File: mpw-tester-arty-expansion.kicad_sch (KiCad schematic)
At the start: 111 parts

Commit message: Update MCP4661 symbol
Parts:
- removed J?: 61300611121, antmicro-footprints:61300611121, symbol antmicroRectangularConnectorsHeadersMalePins:61300611121
- removed U?: MCP4661, antmicro-footprints:QFN-16_EP_4x4_Pitch0.65mm, symbol antmicroInterfaceIOExpanders:MCP4661
- added J?: 61300611121, antmicro-footprints:61300611121, symbol antmicroRectangularConnectorsHeadersMalePins:61300611121
- added U?: MCP4661-103E/ML, antmicro-footprints:QFN-16_EP_4x4_Pitch0.65mm, symbol antmicroInterfaceIOExpanders:MCP4661-103E/ML
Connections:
- net AGND: now also U?.10 (P0B), U?.13 (A2), U?.14 (A1), U?.3 (VSS), U?.4 (VSS), U?.5 (P1B)
- net ARTY_SCL: now also U?.1 (SCL)
- net ARTY_SDA: now also U?.2 (SDA)
- net MEM.SCK: now also J?.2
- net MEM.SI: now also J?.3
- net MEM.SO: now also J?.4
- net MEM.~{CS}: now also J?.1
- net MEM.~{HOLD}: now also J?.6
- net MEM.~{WP}: now also J?.5
- net P0W: now also U?.9 (P0W)
- net P1W: now also U?.6 (P1W)
- net 5V0_SEL: now reaches C?.1, J?.1, R?.1, R?.1, R?.1, R?.1, R?.2, U?.1 (VIN)
- net 5V0_SEL: now also U?.15 (VDD)
- net at R?.1: now also U?.12 (~{WP})
- net at R?.2: now also U?.16 (HVC/A0)
- net 5V0: now reaches D?.K, D?.K, J?.2
- net 5V_ARTY renamed 5V0_ARTY
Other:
- moved on the sheet: C?, D?, J?, R?, U?

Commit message: Cleanup net names
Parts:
- removed J?: Conn_01x02, Connector_PinHeader_2.54mm:PinHeader_1x02_P2.54mm_Vertical, symbol Connector_Generic:Conn_01x02
- removed J?: 61300611121, antmicro-footprints:61300611121, symbol antmicroRectangularConnectorsHeadersMalePins:61300611121
- added C? (x2): C_100n_0402, antmicro-footprints:0402-cap, symbol antmicroCapacitors0402:C_100n_0402
- added C?: C_1u_0402, antmicro-footprints:0402-cap, symbol antmicroCapacitors0402:C_1u_0402
- added J?: 61300711121, antmicro-footprints:61300711121, symbol antmicroRectangularConnectorsHeadersMalePins:61300711121
- added J?: 61300311121, antmicro-footprints:PinHeader_1x3_P2.54_Drill1.1mm, symbol antmicroRectangularConnectorsHeadersMalePins:61300311121
- added NT? (x2): NetTie_2, antmicro-footprints:NetTie-2_SMD_Pad0.127mm, symbol antmicroShuntsJumpers:NetTie_2
- added U?: NTS0102GT, antmicro-footprints:PSON50P100X195X50-8N, symbol antmicroLogicTranslatorsLevelShifters:NTS0102GT
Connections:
- net gpio is gone; now on net CRVL_~{RST}: J?.4
- net ~{RST} is gone; now on net CRVL_GPIO: J?.2
- net +3V3: no longer J?.1
- net 5V0_SEL: now also C?.1, U?.7 (VCC_B)
- net AGND: now also C?.2, C?.2, C?.2, J?.7, U?.2 (GND)
- net ARTY_SCL: now also U?.8 (B1); no longer J?.47 (SCL)
- net ARTY_SDA: now also U?.1 (B2); no longer J?.48 (SDA)
- net ARTY_XCLK: now also J?.1
- net MEM.SCK: now also J?.2
- net MEM.SI: now also J?.3
- net MEM.SO: now also J?.4
- net MEM.~{CS}: now also J?.1
- net MEM.~{HOLD}: now also J?.6
- net MEM.~{WP}: now also J?.5
- net MPRJ_IO[6]_SER_TX: no longer J?.2, NT?.1, U?.36 (TX_IO6)
- net USB_CS1: now also NT?.2; no longer NT?.2
- net USB_SCK_TXD: now also NT?.2; no longer NT?.2
- net USB_SI: now also NT?.2; no longer NT?.2
- net USB_SO_RXD: no longer U?.4 (Y)
- net VDDIO: now also J?.1
- net XCLK_10MHz: now also J?.3; no longer U?.52 (XCLK)
- net 3V3_ARTY: now reaches J?.4 (3.3V)
- net 3V3_ARTY: now also C?.1, C?.1, U?.3 (VCC_A), U?.6 (OE)
- net CARAVEL_GPIO renamed CRVL_GPIO
- net CARAVEL_~{RST} renamed CRVL_~{RST}
- net MPRJ_IO[0] renamed CRVL_IO0
- net MPRJ_IO[10] renamed CRVL_IO10
- net MPRJ_IO[11] renamed CRVL_IO11
- net MPRJ_IO[12] renamed CRVL_IO12
- net MPRJ_IO[13] renamed CRVL_IO13
- net MPRJ_IO[14] renamed CRVL_IO14
- net MPRJ_IO[15] renamed CRVL_IO15
- net MPRJ_IO[16] renamed CRVL_IO16
- net MPRJ_IO[17] renamed CRVL_IO17
- net MPRJ_IO[18] renamed CRVL_IO18
- net MPRJ_IO[19] renamed CRVL_IO19
- net MPRJ_IO[1]_SDO renamed CRVL_IO1
- net CRVL_IO1: now also NT?.1; no longer NT?.1
- net MPRJ_IO[20] renamed CRVL_IO20
- net MPRJ_IO[21] renamed CRVL_IO21
- net MPRJ_IO[22] renamed CRVL_IO22
- net MPRJ_IO[23] renamed CRVL_IO23
- net MPRJ_IO[24] renamed CRVL_IO24
- net MPRJ_IO[25] renamed CRVL_IO25
- net MPRJ_IO[26] renamed CRVL_IO26
- net MPRJ_IO[27] renamed CRVL_IO27
- net MPRJ_IO[28] renamed CRVL_IO28
- net MPRJ_IO[29] renamed CRVL_IO29
- net MPRJ_IO[2]_SDI renamed CRVL_IO2
- net MPRJ_IO[30] renamed CRVL_IO30
- net MPRJ_IO[31] renamed CRVL_IO31
- net MPRJ_IO[32] renamed CRVL_IO32
- net MPRJ_IO[33] renamed CRVL_IO33
- net MPRJ_IO[34] renamed CRVL_IO34
- net MPRJ_IO[35] renamed CRVL_IO35
- net MPRJ_IO[36] renamed CRVL_IO36
- net MPRJ_IO[37] renamed CRVL_IO37
- net MPRJ_IO[3]_CSB renamed CRVL_IO3
- net CRVL_IO3: now also NT?.1; no longer NT?.1
- net MPRJ_IO[4]_SCK renamed CRVL_IO4
- net CRVL_IO4: now also NT?.1; no longer NT?.1
- net MPRJ_IO[5]_SER_RX renamed CRVL_IO5
- net CRVL_IO5: now also NT?.1; no longer J?.3
- net MPRJ_IO[7] renamed CRVL_IO7
- net MPRJ_IO[8] renamed CRVL_IO8
- net MPRJ_IO[9] renamed CRVL_IO9
- net xclk renamed CRVL_XCLK
- net CRVL_XCLK: now also U?.52 (XCLK), J?.2
- new net ARTY_SCL_3V3: J?.47 (SCL), U?.5 (A1)
- new net ARTY_SDA_3V3: J?.48 (SDA), U?.4 (A2)
- new net CRVL_IO6: NT?.1, NT?.1, U?.36 (TX_IO6), U?.4 (Y)
- new net CRVL_RX: J?.3, NT?.2
- new net CRVL_TX: J?.2, NT?.2
- no-connect marks 25 -> 24
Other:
- note added: "XCLK SELECT"
- note removed: "Arty Interface with Caravel"
- note removed: "EXTERNAL XCLK SELECT"
- moved on the sheet: C?, D?, J?, J?A, R?, Y?

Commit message: Cleanup configurable LDO section
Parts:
- removed J?: 61300211121, antmicro-footprints:PinHeader_1x2_P2.54_Drill0.9mm, symbol antmicroRectangularConnectorsHeadersMalePins:61300211121
- removed R?: R_16k2_0402, antmicro-footprints:0402-res, symbol antmicroResistors0402:R_16k2_0402
- removed R? (x4): R_10k_0402, antmicro-footprints:0402-res, symbol antmicroResistors0402:R_10k_0402
- removed R?: R_4k7_0402, antmicro-footprints:0402-res, symbol antmicroResistors0402:R_4k7_0402
- removed R?: R_4k42_0402, antmicro-footprints:0402-res, symbol antmicroResistors0402:R_4k42_0402
- added J?: 61300211121, antmicro-footprints:PinHeader_1x2_P2.54_Drill0.9mm, symbol antmicroRectangularConnectorsHeadersMalePins:61300211121
- added R? (x4): R_10k_0402, antmicro-footprints:0402-res, symbol antmicroResistors0402:R_10k_0402
- added R?: R_4k7_0402, antmicro-footprints:0402-res, symbol antmicroResistors0402:R_4k7_0402
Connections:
- net P0W is gone; now on net ADJ1: U?.9 (P0W)
- net 5V0_SEL: now also R?.1
- net ADJ2: now also U?.6 (P1W)
- net AGND: now also R?.1, R?.1; no longer U?.10 (P0B), U?.5 (P1B)
- net ARTY_SCL: now also R?.2
- net VOUT1: now also R?.2
- net VOUT2: now also R?.2
- net P1A: now reaches U?.7 (P1A)
- net P1A: now also J?.1, R?.1
- net P0A: now reaches U?.8 (P0A)
- net P0A: now also J?.1, R?.1
- net P1W renamed P0B
- net P0B: now also U?.10 (P0B), R?.2; no longer U?.6 (P1W)
- new net P1B: J?.2, R?.2, U?.5 (P1B)
- no-connect marks 24 -> 22
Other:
- note added: "Note: internal pullups in NTS0102GT"
- note added: "TODO: determine feedback resistors values"
- note removed: "Note: I2C pullup on Arty A7"
- moved on the sheet: C?, J?, R?

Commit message: Replace 0603 and 0805 100n and 18p capacitors with 0402
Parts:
- removed C? (x9): 0.1uf - CC0805KRX7R9BB104, Capacitor_SMD:C_0805_2012Metric, symbol antmicroCapacitors0603:C_100n_0603
- removed C? (x2): C_18p_0603, antmicro-footprints:0603-cap, symbol antmicroCapacitors0603:C_18p_0603
- added C1, C11, C13, C14, C15, C16, C5, C7, C8: C_100n_0402, antmicro-footprints:0402-cap, symbol antmicroCapacitors0402:C_100n_0402
- added C6, C9: C_18p_0402, antmicro-footprints:0402-cap, symbol antmicroCapacitors0402:C_18p_0402
- U7: renamed from U?; footprint Caravel_Board:caravel_breakout_flexy -> antmicro-footprints:caravel_breakout
- gave numbers to parts that had none: 101
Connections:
- net AGND: now also C1.2, C11.2, C13.2, C14.2, C15.2, C16.2, C5.2, C6.2, C7.2, C8.2, C9.2
- net FTDI_3V3: now also C1.1, C13.1, C15.1, C16.1, C5.1, C8.1
- net VBUS: now also C7.1
- net VCCA: now also C14.1
- net VCORE: now also C11.1
- net XIN: now also C6.1
- net XOUT: now also C9.1
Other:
- moved on the sheet: R18, Y1

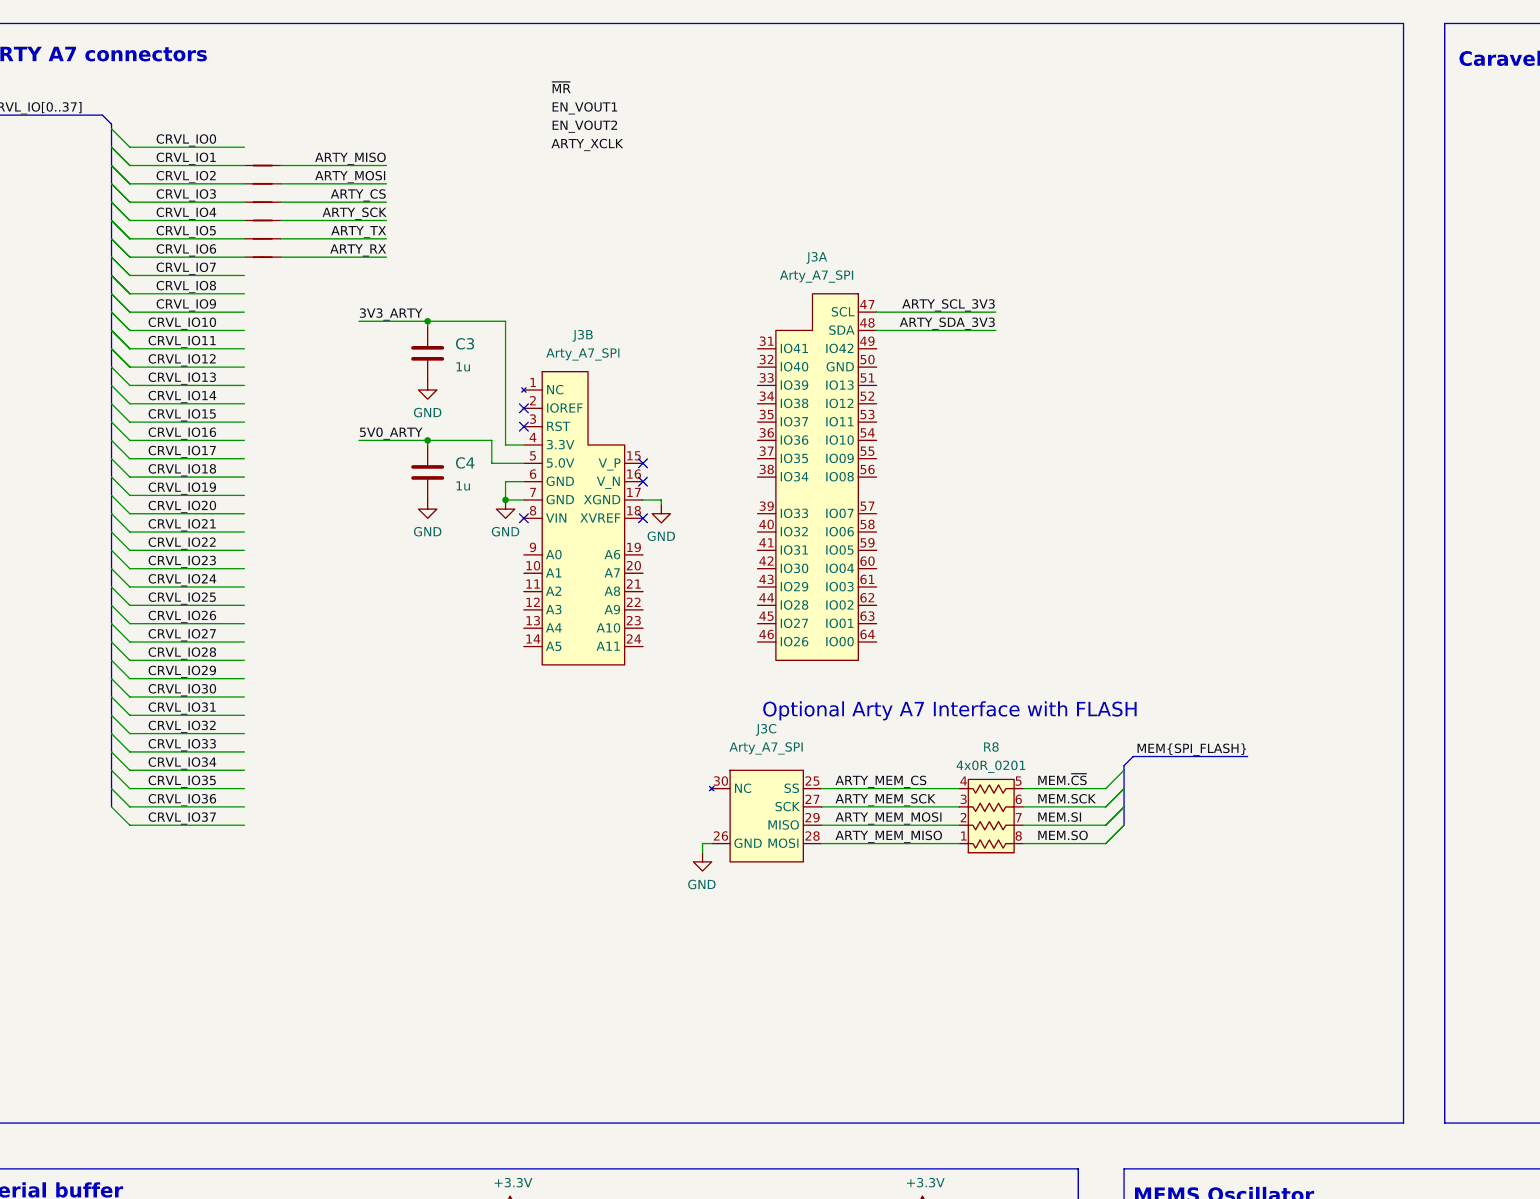
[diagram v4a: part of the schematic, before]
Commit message: Start connecting Caravel to Arty
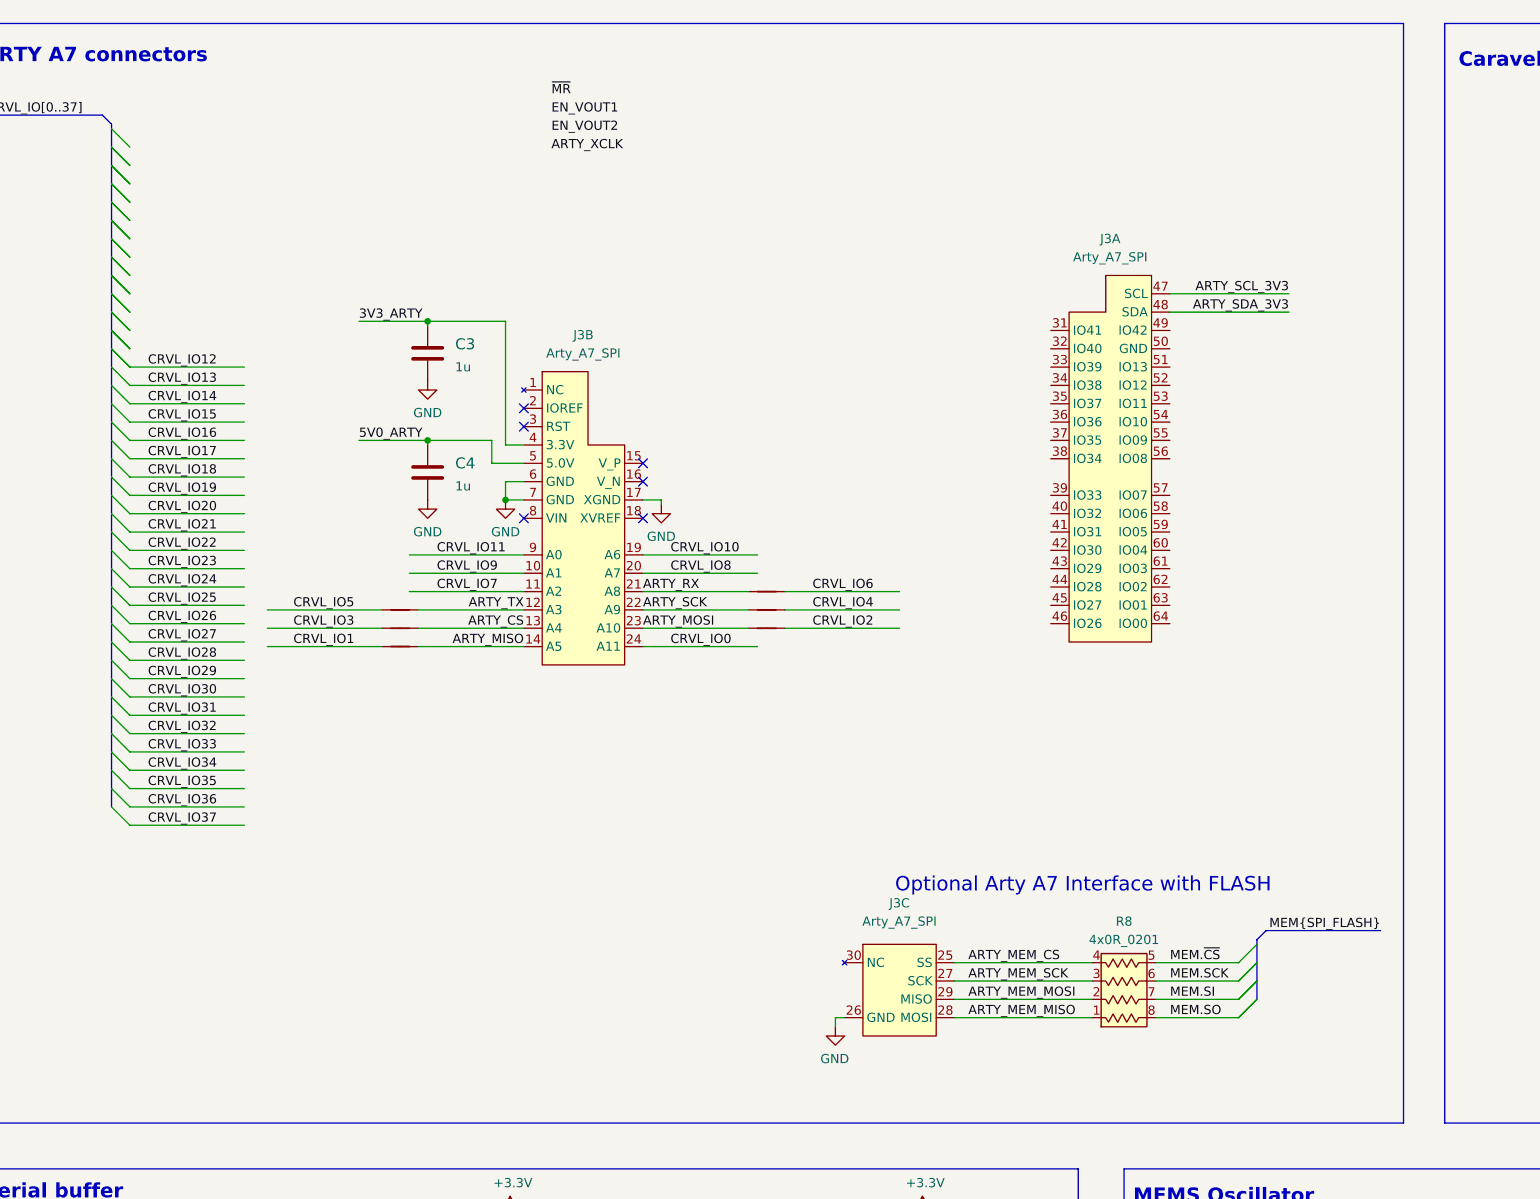
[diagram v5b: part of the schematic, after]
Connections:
- net ARTY_CS: now also J3.13 (A4)
- net ARTY_MISO: now also J3.14 (A5)
- net ARTY_MOSI: now also J3.23 (A10)
- net ARTY_RX: now also J3.21 (A8)
- net ARTY_SCK: now also J3.22 (A9)
- net ARTY_TX: now also J3.12 (A3)
- net CRVL_IO0: now also J3.24 (A11)
- net CRVL_IO10: now also J3.19 (A6)
- net CRVL_IO11: now also J3.9 (A0)
- net CRVL_IO7: now also J3.11 (A2)
- net CRVL_IO8: now also J3.20 (A7)
- net CRVL_IO9: now also J3.10 (A1)
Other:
- moved on the sheet: J3A, J3C, R8

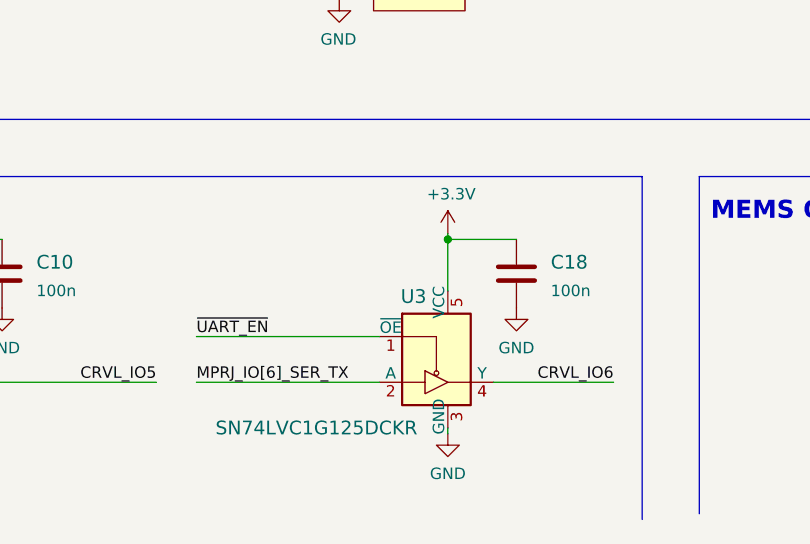
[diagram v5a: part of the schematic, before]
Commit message: Fix signals label on U3. Power U3 from FTDI 3V3
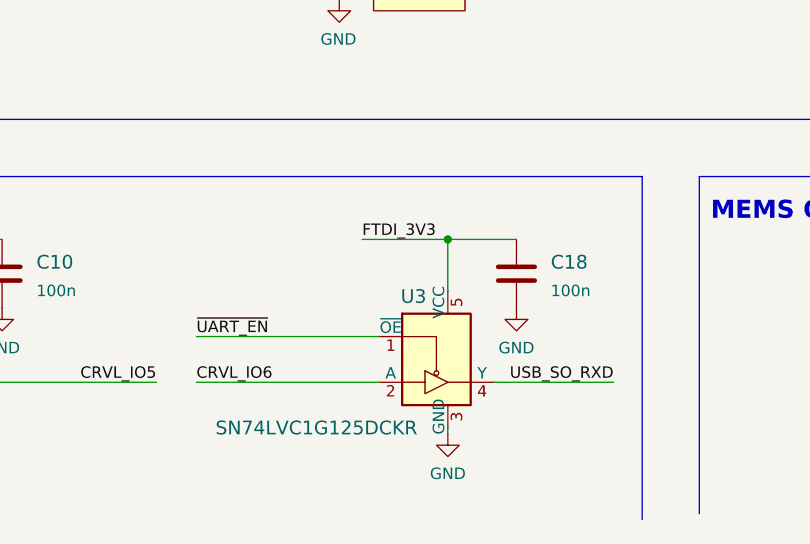
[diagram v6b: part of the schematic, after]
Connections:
- net MPRJ_IO[6]_SER_TX is gone; now on net CRVL_IO6: U3.2 (A)
- net +3V3: no longer C18.1, U3.5 (VCC)
- net CRVL_IO6: no longer U3.4 (Y)
- net FTDI_3V3: now also C18.1, U3.5 (VCC)
- net USB_SO_RXD: now also U3.4 (Y)
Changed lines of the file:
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@@
     (rev "0.0.99")
   )
-  (bus_alias "SPI_FLASH" (members "~{CS}" "SCK" "SI" "SO" "~{WP}" "~{HOLD}"))
   (bus_alias "SPI" (members "~{CS}" "MISO" "MOSI" "SCK"))
+  (bus_alias "SPI_FLASH" (members "~{CS}" "SCK" "SI" "SO" "~{WP}" "~{HOLD}"))
   (junction (at 122.555 74.93) (diameter 0) (color 0 0 0 0)
   )
@@
     (stroke (width 0) (type default) (color 0 0 0 0))
   )
+  (wire (pts (xy 143.51 311.785) (xy 133.985 311.785))
+    (stroke (width 0) (type default) (color 0 0 0 0))
+  )
   (wire (pts (xy 309.245 205.105) (xy 309.245 211.455))
     (stroke (width 0) (type default) (color 0 0 0 0))
@@
     (stroke (width 0) (type default) (color 0 0 0 0))
   )
-  (wire (pts (xy 143.51 311.15) (xy 143.51 311.785))
-    (stroke (width 0) (type default) (color 0 0 0 0))
-  )
   (wire (pts (xy 177.8 183.515) (xy 194.31 183.515))
     (stroke (width 0) (type default) (color 0 0 0 0))
@@
     (effects (font (size 1.27 1.27)) (justify left bottom))
   )
-  (label "CRVL_IO6" (at 161.925 327.66 180)
-    (effects (font (size 1.27 1.27)) (justify right bottom))
+  (label "CRVL_IO6" (at 115.57 327.66 0)
+    (effects (font (size 1.27 1.27)) (justify left bottom))
   )
   (label "FTDI_3V3" (at 79.375 85.09 0)
@@
     (effects (font (size 1.27 1.27)) (justify left bottom))
   )
-  (label "MPRJ_IO[6]_SER_TX" (at 115.57 327.66 0)
-    (effects (font (size 1.27 1.27)) (justify left bottom))
-  )
   (label "CRVL_IO22" (at 45.72 219.075 180)
     (effects (font (size 1.27 1.27)) (justify right bottom))
@@
     (effects (font (size 1.27 1.27)) (justify right bottom))
   )
+  (label "USB_SO_RXD" (at 161.925 327.66 180)
+    (effects (font (size 1.27 1.27)) (justify right bottom))
+  )
   (label "ARTY_XCLK" (at 321.31 247.015 180)
     (effects (font (size 1.27 1.27)) (justify right bottom))
@@
     (effects (font (size 1.27 1.27)) (justify left bottom))
   )
+  (label "FTDI_3V3" (at 133.985 311.785 0)
+    (effects (font (size 1.27 1.27)) (justify left bottom))
+  )
   (label "MEM{SPI_FLASH}" (at 494.03 73.025 0)
     (effects (font (size 1.27 1.27)) (justify left bottom))
@@
     (pin "2")
   )
-  (symbol (lib_id "power:+3.3V") (at 143.51 311.15 0) (unit 1)
-    (in_bom yes) (on_board yes)
-    (property "Reference" "#PWR0151" (id 0) (at 143.51 314.96 0)
-      (effects (font (size 1.27 1.27)) hide)
-    )
-    (property "Value" "+3.3V" (id 1) (at 143.891 306.7558 0))
-    (property "Footprint" "" (id 2) (at 143.51 311.15 0)
-      (effects (font (size 1.27 1.27)) hide)
-    )
-    (property "Datasheet" "" (id 3) (at 143.51 311.15 0)
-      (effects (font (size 1.27 1.27)) hide)
-    )
-    (pin "1")
-  )
   (symbol (lib_id "antmicroCapacitors0402:C_18p_0402") (at 90.805 127 0) (unit 1)
     (in_bom yes) (on_board yes) (fields_autoplaced)
@@
       (reference "#PWR0150") (unit 1) (value "GND") (footprint "")
     )
-    (path "/ad92e2ba-93ce-4b21-a047-ccc26513a106"
-      (reference "#PWR0151") (unit 1) (value "+3.3V") (footprint "")
-    )
     (path "/3349caa0-d316-426d-823b-0e2b9b5356e8"
